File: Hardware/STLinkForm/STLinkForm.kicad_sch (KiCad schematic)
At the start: 68 parts, among them J1 USB_B_Micro, J2 JTAG, J3 RS232, J4 ISP, J5 SWD, U1 SRV05-4, U2 STM32F103CBT6, U3 HT7833, U4 74LS125, U5 74LS125, U6 AD8531ARTZ, U7 SRV05-4, U8 74LVCH2T45DC, U9 SRV05-4, Y1 8MHz

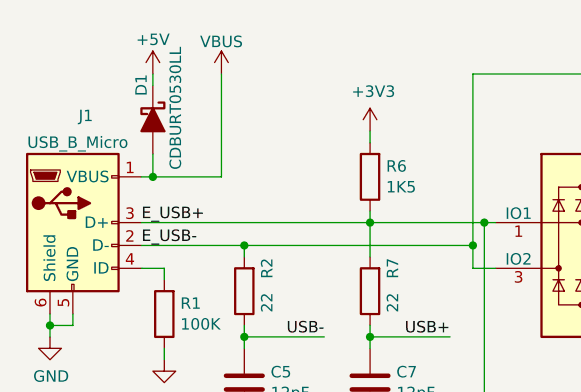
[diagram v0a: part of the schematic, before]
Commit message: Changed input diode to 1A
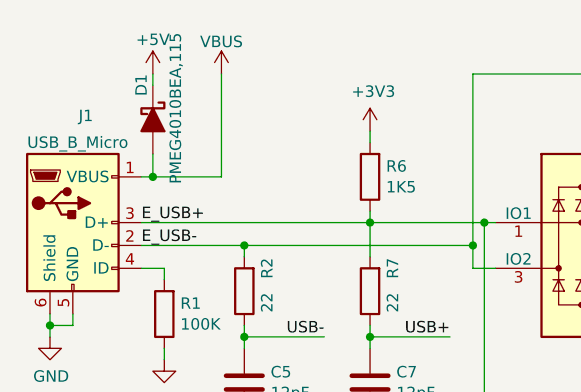
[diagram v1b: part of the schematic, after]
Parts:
- D1: value CDBURT0530LL -> PMEG4010BEA,115; footprint Diode_SMD:D_0603_1608Metric_Pad1.05x0.95mm_HandSolder -> Diode_SMD:D_SOD-323_HandSoldering
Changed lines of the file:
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@@
       (effects (font (size 1.27 1.27)) (justify left))
     )
-    (property "Value" "CDBURT0530LL" (id 1) (at 30.48 21.59 0))
-    (property "Footprint" "Diode_SMD:D_0603_1608Metric_Pad1.05x0.95mm_HandSolder" (id 2) (at 27.94 22.86 0)
+    (property "Value" "PMEG4010BEA,115" (id 1) (at 30.48 21.59 0))
+    (property "Footprint" "Diode_SMD:D_SOD-323_HandSoldering" (id 2) (at 27.94 22.86 0)
       (effects (font (size 1.27 1.27)) hide)
     )
@@
     )
     (path "/00000000-0000-0000-0000-000060e47edd"
-      (reference "D1") (unit 1) (value "CDBURT0530LL") (footprint "Diode_SMD:D_0603_1608Metric_Pad1.05x0.95mm_HandSolder")
+      (reference "D1") (unit 1) (value "PMEG4010BEA,115") (footprint "Diode_SMD:D_SOD-323_HandSoldering")
     )
     (path "/9ac1bd70-9a82-4008-b127-38e4175b24af"

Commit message: Final review of 'Glossy-MSP430 STLink Form' and fabrication output.
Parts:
- NT1: symbol STLinkForm-rescue:Net-Tie_2-Device -> Device:NetTie_2
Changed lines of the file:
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@@
   (title_block
     (title "The Glossy MSP430 (STLink Form)")
-    (date "2022-12-04")
+    (date "2022-12-08")
     (rev "2")
     (company "Mathias Gruber")
@@
     (pin "2")
   )
-  (symbol (lib_id "STLinkForm-rescue:Net-Tie_2-Device") (at 156.21 41.91 180) (unit 1)
+  (symbol (lib_id "Device:NetTie_2") (at 156.21 41.91 180) (unit 1)
     (in_bom yes) (on_board yes)
     (property "Reference" "NT1" (id 0) (at 154.94 40.64 0)
@@
       (effects (font (size 1.27 1.27)) (justify right) hide)
     )
-    (property "Footprint" "NetTie:NetTie-2_SMD_Pad0.5mm" (id 2) (at 157.988 41.91 90)
-      (effects (font (size 1.27 1.27)) hide)
-    )
+    (property "Footprint" "NetTie:NetTie-2_SMD_Pad0.5mm" (id 2) (at 156.21 41.91 0)
+      (effects (font (size 1.27 1.27)) hide)
+    )
